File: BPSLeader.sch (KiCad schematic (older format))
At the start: 25 parts, among them J1 GPIO Analyzer, J2 Volt/Temp SPI Analyzer, J3 Current SPI Analyzer, J4 CAN Analyzer, J5 SWD, SW1 B3SL-1002P, U1 STM32F413RHTx, Y1 8M

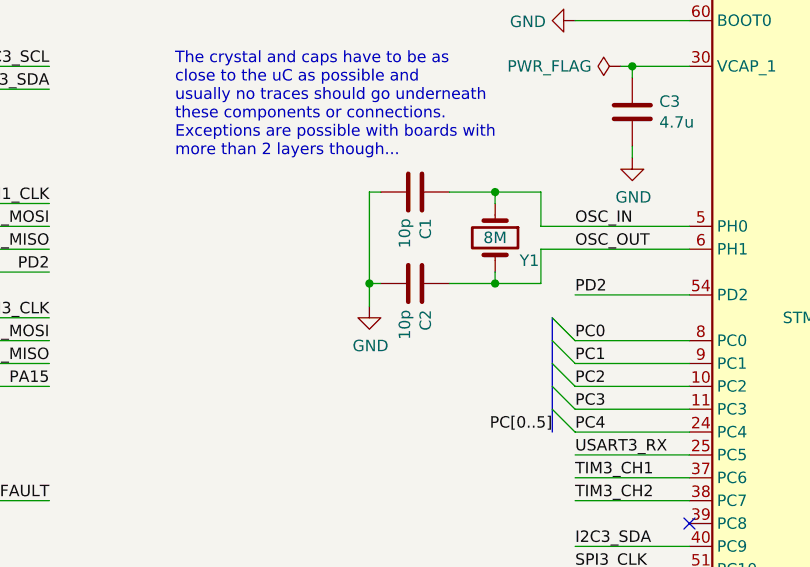
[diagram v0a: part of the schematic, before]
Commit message: Moves BAS70-04 to utsvt-chips because other systems use this component
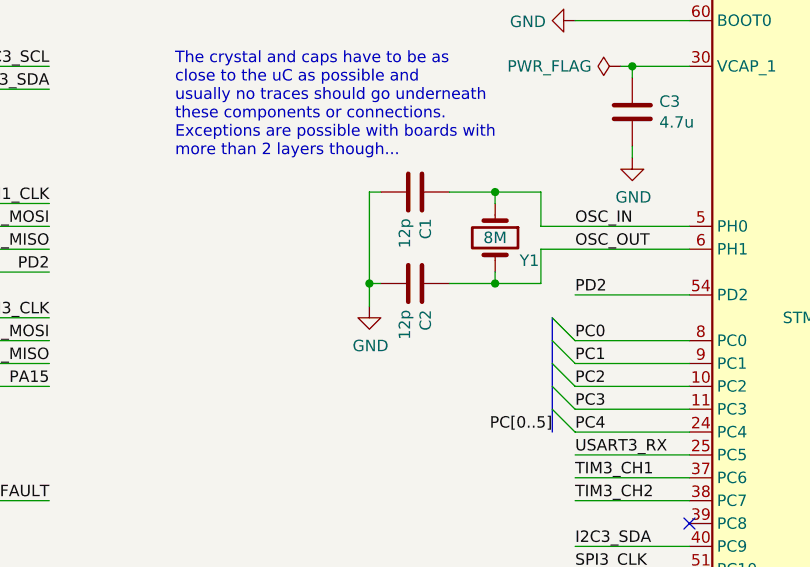
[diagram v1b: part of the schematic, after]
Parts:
- C1, C2: value 10p -> 12p
- Y1: P/N CRYSTAL 8.0000MHZ 18PF SMD -> 7A-8.000MAHJ-T
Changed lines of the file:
@@
 F 1 "8M" V 4250 3550 50  0000 C CNN
 F 2 "Crystal:Crystal_SMD_TXC_7A-2Pin_5x3.2mm" H 4250 3550 50  0001 C CNN
-F 3 "~" H 4250 3550 50  0001 C CNN
-F 4 "CRYSTAL 8.0000MHZ 18PF SMD" H 4250 3550 50  0001 C CNN "P/N"
+F 3 "https://www.mouser.com/datasheet/2/417/7a-13881.pdf" H 4250 3550 50  0001 C CNN
+F 4 "7A-8.000MAHJ-T" H 4250 3550 50  0001 C CNN "P/N"
 	1    4250 3550
 	0    1    1    0
@@
 P 3900 3750
 F 0 "C2" H 4015 3796 50  0000 L CNN
-F 1 "10p" H 4015 3705 50  0000 L CNN
+F 1 "12p" H 4015 3705 50  0000 L CNN
 F 2 "Capacitor_SMD:C_0805_2012Metric" H 3938 3600 50  0001 C CNN
 F 3 "~" H 3900 3750 50  0001 C CNN
@@
 P 3900 3350
 F 0 "C1" H 4015 3396 50  0000 L CNN
-F 1 "10p" H 4015 3305 50  0000 L CNN
+F 1 "12p" H 4015 3305 50  0000 L CNN
 F 2 "Capacitor_SMD:C_0805_2012Metric" H 3938 3200 50  0001 C CNN
 F 3 "~" H 3900 3350 50  0001 C CNN
